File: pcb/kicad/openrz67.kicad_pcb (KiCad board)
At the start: 2 copper layers, 48 x 22 mm, 62 parts, among them J1 GPIO header, Q3 AO3401A, U1 ESP32-C3FH4, U2 TPS63031DSKR, U3 BQ25185DLHR, U4 S4B-XH-A(LF)(SN), U5 TLP172AM, U6 TLP172AM, X1 40MHz, X2 32.768kHz

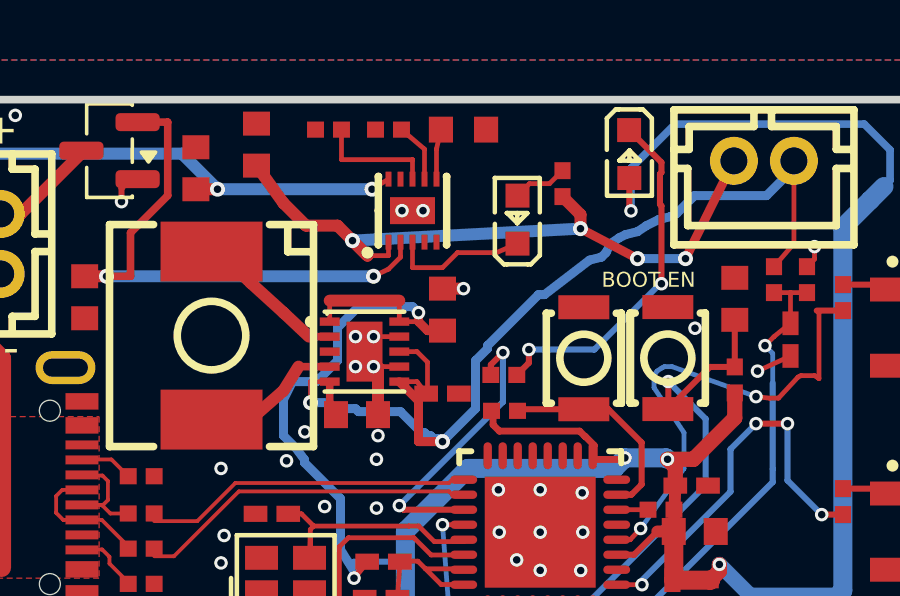
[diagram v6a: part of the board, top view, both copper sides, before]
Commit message: PCB rev 3: C24 at U2 pin 1 (VOUT), not pin 10 (FB); reversed cell with USB documented
PR #9 review: VOUT is pin 1, pin 10 is FB tied to VOUT, so the first move only
got the cap to the FB side. C24 now at (134.15, 95.9), VCC pad 0.8 mm from pin 1,
in the notch between L3 and the VSYS corner; the VSYS via moved 0.3 mm east to
make room. Return GND via beside its GND pad. README: with USB in, the charger
turns Q3 on regardless of cell polarity and trickles ~7 mA into a reversed cell
until the safety timer; unplug USB first. DRC 0 err / 22 warn (+2 courtyard,
+4 silk clipped by mask at C24), ERC unchanged.
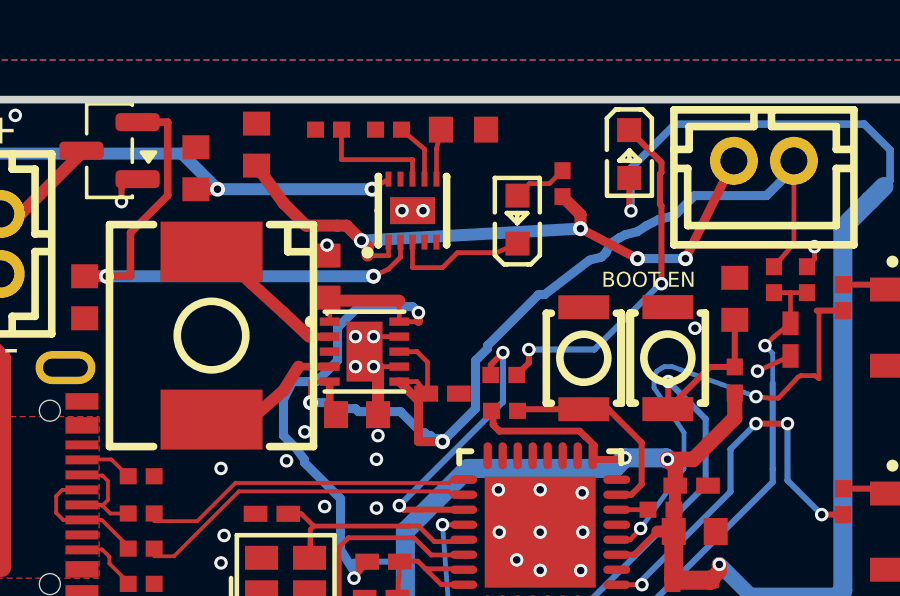
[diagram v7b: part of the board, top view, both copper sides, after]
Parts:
- moved C24 4.00 mm to (134.2, 95.9)
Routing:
- net VCC: track 114.1 -> 113.2 mm
- net VSYS: track 23.2 -> 22.4 mm
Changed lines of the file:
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@@
 	(footprint "openrz67:C0603"
 		(layer "F.Cu")
-		(at 138 97 -90)
+		(at 134.15 95.9 -90)
 		(property "Reference" "C24"
 			(at 2.87 1.0235 0)
@@
 	)
 	(segment
-		(start 138 96.3)
-		(end 138.7 96.3)
-		(width 0.4)
-		(layer "F.Cu")
-		(net "GND")
-	)
-	(segment
 		(start 135.85 100.5)
 		(end 135.85 99)
@@
 		(net "GND")
 	)
+	(segment
+		(start 134.15 95.2)
+		(end 134.15 94.85)
+		(width 0.3)
+		(layer "F.Cu")
+		(net "GND")
+	)
 	(via
 		(at 128.232 107.221)
@@
 	)
 	(via
+		(at 134.15 94.85)
+		(size 0.45)
+		(drill 0.25)
+		(layers "F.Cu" "B.Cu")
+		(net "GND")
+	)
+	(via
 		(at 139.5295 109.101)
 		(size 0.45)
@@
 	)
 	(via
-		(at 138.7 96.3)
-		(size 0.45)
-		(drill 0.25)
-		(layers "F.Cu" "B.Cu")
-		(net "GND")
-	)
-	(via
 		(at 138.339 110.269)
 		(size 0.45)
@@
 	)
 	(segment
-		(start 137.5 97.7)
-		(end 138 97.7)
-		(width 0.3)
-		(layer "F.Cu")
-		(net "VCC")
-	)
-	(segment
 		(start 146.9395 106.007)
 		(end 147.229 105.7175)
@@
 	)
 	(segment
-		(start 137.2 97.4)
-		(end 137.5 97.7)
-		(width 0.3)
-		(layer "F.Cu")
-		(net "VCC")
-	)
-	(segment
 		(start 139.8955 101.0495)
 		(end 139.6855 100.84)
@@
 		(net "VCC")
 	)
+	(segment
+		(start 134.15 96.7)
+		(end 134.24 96.7)
+		(width 0.3)
+		(layer "F.Cu")
+		(net "VCC")
+	)
 	(via
 		(at 137.577 107.831)
@@
 	)
 	(segment
-		(start 135.5 95.2)
-		(end 134.5 94.2)
+		(start 135.3 94.7)
+		(end 135.5 94.9)
+		(width 0.4)
+		(layer "F.Cu")
+		(net "VSYS")
+	)
+	(segment
+		(start 135.5 94.9)
+		(end 135.5 95.2)
 		(width 0.4)
 		(layer "F.Cu")
@@
 	)
 	(segment
+		(start 134.8 94.2)
+		(end 135.3 94.7)
+		(width 0.4)
+		(layer "F.Cu")
+		(net "VSYS")
+	)
+	(segment
 		(start 142.6 93.833)
 		(end 142 93.233)
@@
 	)
 	(segment
-		(start 135.5 95.2)
-		(end 135 94.7)
+		(start 134.5 94.2)
+		(end 134.8 94.2)
 		(width 0.4)
 		(layer "F.Cu")
@@
 	)
 	(via
-		(at 135 94.7)
+		(at 135.3 94.7)
 		(size 0.5)
-		(drill 0.25)
+		(drill 0.3)
 		(layers "F.Cu" "B.Cu")
 		(net "VSYS")
@@
 	)
 	(segment
-		(start 135 94.7)
+		(start 135.3 94.7)
 		(end 142.6 94.3)
 		(width 0.4)
